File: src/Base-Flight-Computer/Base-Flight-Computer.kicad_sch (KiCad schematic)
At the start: 50 parts, among them J1 Jumper_NO, P1 1984659, P2 USB, P3 0530470610, P4 1546551-2, Q1 QS5U17TR, Q2 2N7002W-7-F, Q3 2N7002W-7-F, Q4 QS5U17TR, U1 STM32G4A1KEU6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

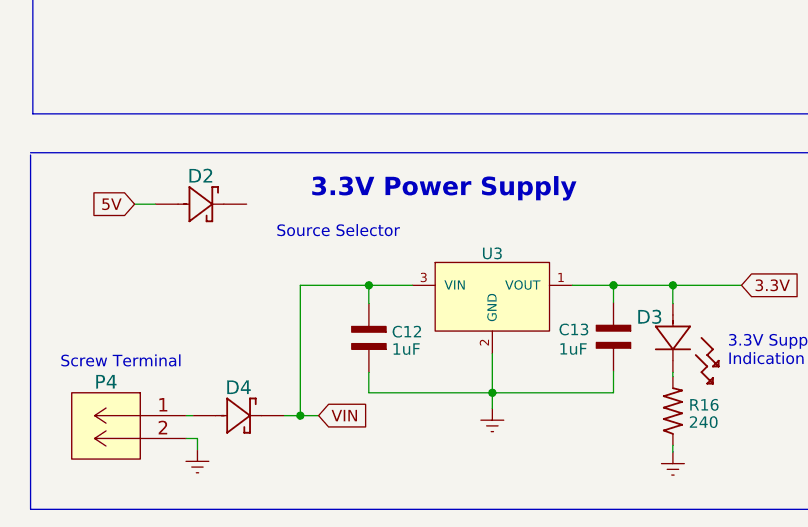
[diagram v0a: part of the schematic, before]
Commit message: added lipo batter connector to power supply circuit
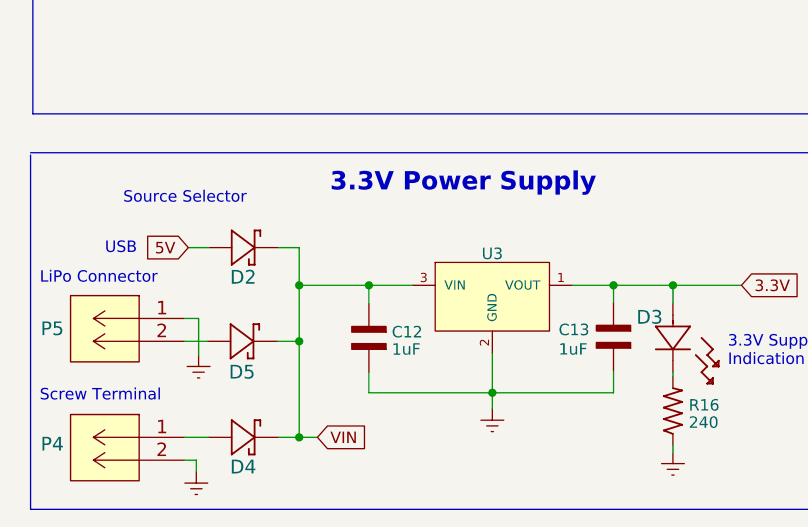
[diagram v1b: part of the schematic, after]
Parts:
- removed D2, D4: SM5819PL-TP, symbol Flight-Computer:SM5819PL-TP
- added D2, D4, D5: SM5819PL-TP, Base-Flight-Computer:SM5819PL-TP, symbol Base-Flight-Computer:SM5819PL-TP
- added P5: 1984659, Base-Flight-Computer:JST_S2B-PH-K-S(LF)(SN), symbol Base-Flight-Computer:S2B-PH-K-S__LF__SN
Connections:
- net 5V: now also D2.2
- net Earth: now also P5.1 (5)
- net VIN: now also D2.1, D4.1, D5.1
- net at P4.1 (5): now also D4.2
- new net: D5.2, P5.2 (6)
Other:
- note added: "LiPo Connector"
- moved on the sheet: P4

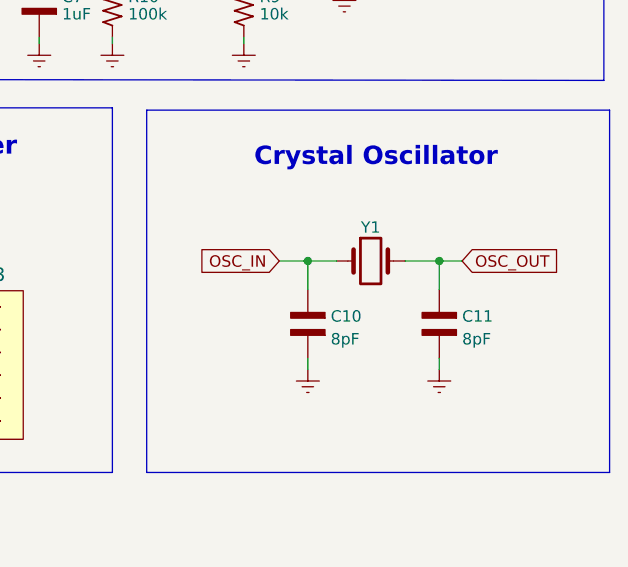
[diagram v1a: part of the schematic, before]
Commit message: reduced form factor of crystal oscillator
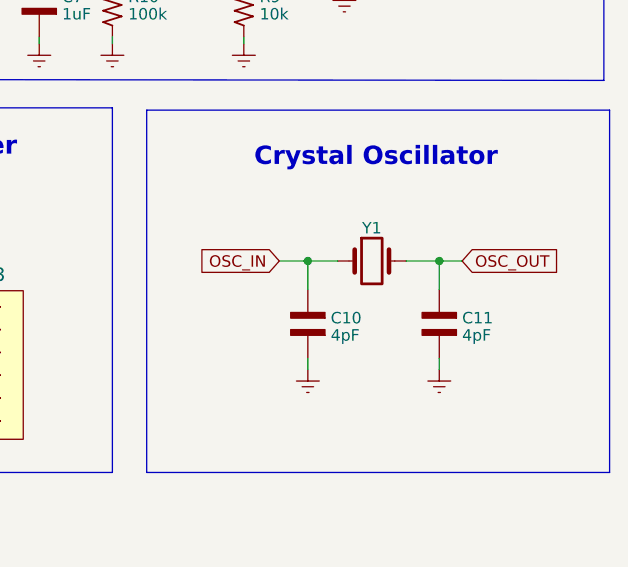
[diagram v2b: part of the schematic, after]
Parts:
- removed C10, C11: 8pF, Flight-Computer-Lite:CAP_0603, symbol Flight-Computer:CAP_0603
- removed Y1: ECS-240-18-33-JGN-TR, Flight-Computer-Lite:ECS-240-18-33-JGN-TR, symbol Flight-Computer:ECS-240-18-33-JGN-TR
- added C10, C11: 4pF, Base-Flight-Computer:CAP_0402, symbol Base-Flight-Computer:CAP_0402
- added Y1: ECS-240-18-33-JGN-TR, Base-Flight-Computer:ECS-240-12-37B-CKY-TR, symbol Base-Flight-Computer:ECS-240-12-37B-CKY-TR
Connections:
- net Earth: now also C10.2, C11.2
- net OSC_IN: now also C10.1, Y1.1
- net OSC_OUT: now also C11.1, Y1.3
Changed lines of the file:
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@@
+    (stroke (width 0) (type default))
+  )
+  (wire (pts (xy 259.969 140.97) (xy 263.652 140.97))
     (stroke (width 0) (type default))
   )
@@
     (stroke (width 0) (type default))
   )
+  (wire (pts (xy 249.047 140.97) (xy 252.349 140.97))
+    (stroke (width 0) (type default))
+  )
   (polyline (pts (xy 114.554 17.018) (xy 172.974 17.018))
     (stroke (width 0) (type default))
@@
     (stroke (width 0) (type default))
   )
-  (wire (pts (xy 259.842 140.97) (xy 263.652 140.97))
-    (stroke (width 0) (type default))
-  )
   (wire (pts (xy 199.136 148.59) (xy 204.724 148.59))
     (stroke (width 0) (type default))
@@
   )
   (wire (pts (xy 80.264 179.832) (xy 66.802 179.832))
-    (stroke (width 0) (type default))
-  )
-  (wire (pts (xy 249.047 140.97) (xy 252.222 140.97))
     (stroke (width 0) (type default))
   )
@@
     )
   )
-  (symbol (lib_id "Flight-Computer:ECS-240-18-33-JGN-TR") (at 256.032 140.97 0) (unit 1)
-    (in_bom yes) (on_board yes) (dnp no) (fields_autoplaced)
-    (property "Reference" "Y1" (at 256.032 137.2418 0)
-      (effects (font (size 1.27 1.27)))
-    )
-    (property "Value" "ECS-240-18-33-JGN-TR" (at 256.032 144.78 0)
-      (effects (font (size 1.27 1.27)) hide)
-    )
-    (property "Footprint" "Flight-Computer-Lite:ECS-240-18-33-JGN-TR" (at 256.032 140.97 0)
-      (effects (font (size 1.27 1.27)) hide)
-    )
-    (property "Datasheet" "~" (at 256.032 140.97 0)
-      (effects (font (size 1.27 1.27)) hide)
-    )
-    (pin "1")
-    (pin "2")
-    (pin "3")
-    (pin "4")
-    (instances
-      (project "Base-Flight-Computer"
-        (path "/13f33ffc-3ab1-449a-9be0-c2c7f72f3b48"
-          (reference "Y1") (unit 1)
-        )
-      )
-    )
-  )
   (symbol (lib_id "Flight-Computer:Earth") (at 227.584 73.152 0) (unit 1)
     (in_bom yes) (on_board yes) (dnp no) (fields_autoplaced)
@@
         (path "/13f33ffc-3ab1-449a-9be0-c2c7f72f3b48"
           (reference "#PWR015") (unit 1)
-        )
-      )
-    )
-  )
-  (symbol (lib_id "Flight-Computer:CAP_0603") (at 249.047 147.955 90) (unit 1)
-    (in_bom yes) (on_board yes) (dnp no) (fields_autoplaced)
-    (property "Reference" "C10" (at 251.587 147.1203 90)
-      (effects (font (size 1.27 1.27)) (justify right))
-    )
-    (property "Value" "8pF" (at 251.587 149.6572 90)
-      (effects (font (size 1.27 1.27)) (justify right))
-    )
-    (property "Footprint" "Flight-Computer-Lite:CAP_0603" (at 259.207 150.495 0)
-      (effects (font (size 1.27 1.27)) (justify left bottom) hide)
-    )
-    (property "Datasheet" "" (at 249.047 149.225 0)
-      (effects (font (size 1.27 1.27)) (justify left bottom) hide)
-    )
-    (pin "1")
-    (pin "2")
-    (instances
-      (project "Base-Flight-Computer"
-        (path "/13f33ffc-3ab1-449a-9be0-c2c7f72f3b48"
-          (reference "C10") (unit 1)
         )
       )
@@
     )
   )
-  (symbol (lib_id "Flight-Computer:CAP_0603") (at 263.652 147.955 90) (unit 1)
-    (in_bom yes) (on_board yes) (dnp no) (fields_autoplaced)
-    (property "Reference" "C11" (at 266.192 147.1203 90)
-      (effects (font (size 1.27 1.27)) (justify right))
-    )
-    (property "Value" "8pF" (at 266.192 149.6572 90)
-      (effects (font (size 1.27 1.27)) (justify right))
-    )
-    (property "Footprint" "Flight-Computer-Lite:CAP_0603" (at 273.812 150.495 0)
-      (effects (font (size 1.27 1.27)) (justify left bottom) hide)
-    )
-    (property "Datasheet" "" (at 263.652 149.225 0)
-      (effects (font (size 1.27 1.27)) (justify left bottom) hide)
-    )
-    (pin "1")
-    (pin "2")
-    (instances
-      (project "Base-Flight-Computer"
-        (path "/13f33ffc-3ab1-449a-9be0-c2c7f72f3b48"
-          (reference "C11") (unit 1)
+  (symbol (lib_id "Base-Flight-Computer:CAP_0402") (at 249.047 147.955 90) (unit 1)
+    (in_bom yes) (on_board yes) (dnp no) (fields_autoplaced)
+    (property "Reference" "C10" (at 251.587 147.3113 90)
+      (effects (font (size 1.27 1.27)) (justify right))
+    )
+    (property "Value" "4pF" (at 251.587 149.2323 90)
+      (effects (font (size 1.27 1.27)) (justify right))
+    )
+    (property "Footprint" "Base-Flight-Computer:CAP_0402" (at 259.207 150.495 0)
+      (effects (font (size 1.27 1.27)) (justify left bottom) hide)
+    )
+    (property "Datasheet" "" (at 249.047 149.225 0)
+      (effects (font (size 1.27 1.27)) (justify left bottom) hide)
+    )
+    (pin "1")
+    (pin "2")
+    (instances
+      (project "Base-Flight-Computer"
+        (path "/13f33ffc-3ab1-449a-9be0-c2c7f72f3b48"
+          (reference "C10") (unit 1)
         )
       )
@@
     )
   )
+  (symbol (lib_id "Base-Flight-Computer:CAP_0402") (at 263.652 147.955 90) (unit 1)
+    (in_bom yes) (on_board yes) (dnp no) (fields_autoplaced)
+    (property "Reference" "C11" (at 266.192 147.3113 90)
+      (effects (font (size 1.27 1.27)) (justify right))
+    )
+    (property "Value" "4pF" (at 266.192 149.2323 90)
+      (effects (font (size 1.27 1.27)) (justify right))
+    )
+    (property "Footprint" "Base-Flight-Computer:CAP_0402" (at 273.812 150.495 0)
+      (effects (font (size 1.27 1.27)) (justify left bottom) hide)
+    )
+    (property "Datasheet" "" (at 263.652 149.225 0)
+      (effects (font (size 1.27 1.27)) (justify left bottom) hide)
+    )
+    (pin "1")
+    (pin "2")
+    (instances
+      (project "Base-Flight-Computer"
+        (path "/13f33ffc-3ab1-449a-9be0-c2c7f72f3b48"
+          (reference "C11") (unit 1)
+        )
+      )
+    )
+  )
   (symbol (lib_id "Base-Flight-Computer:CAP_0402") (at 218.694 68.58 90) (unit 1)
     (in_bom yes) (on_board yes) (dnp no) (fields_autoplaced)
@@
         )
       )
+    )
+  )
+  (symbol (lib_id "Base-Flight-Computer:ECS-240-12-37B-CKY-TR") (at 256.159 140.97 0) (unit 1)
+    (in_bom yes) (on_board yes) (dnp no) (fields_autoplaced)
+    (property "Reference" "Y1" (at 256.159 137.3157 0)
+      (effects (font (size 1.27 1.27)))
+    )
+    (property "Value" "ECS-240-18-33-JGN-TR" (at 256.159 144.78 0)
+      (effects (font (size 1.27 1.27)) hide)
+    )
+    (property "Footprint" "Base-Flight-Computer:ECS-240-12-37B-CKY-TR" (at 256.159 140.97 0)
+      (effects (font (size 1.27 1.27)) hide)
+    )
+    (property "Datasheet" "~" (at 256.159 140.97 0)
+      (effects (font (size 1.27 1.27)) hide)
+    )
+    (pin "1")
+    (pin "2")
+    (pin "3")
+    (pin "4")
+    (instances
+      (project "Base-Flight-Computer"
+        (path "/13f33ffc-3ab1-449a-9be0-c2c7f72f3b48"
+          (reference "Y1") (unit 1)
+        )
+      )

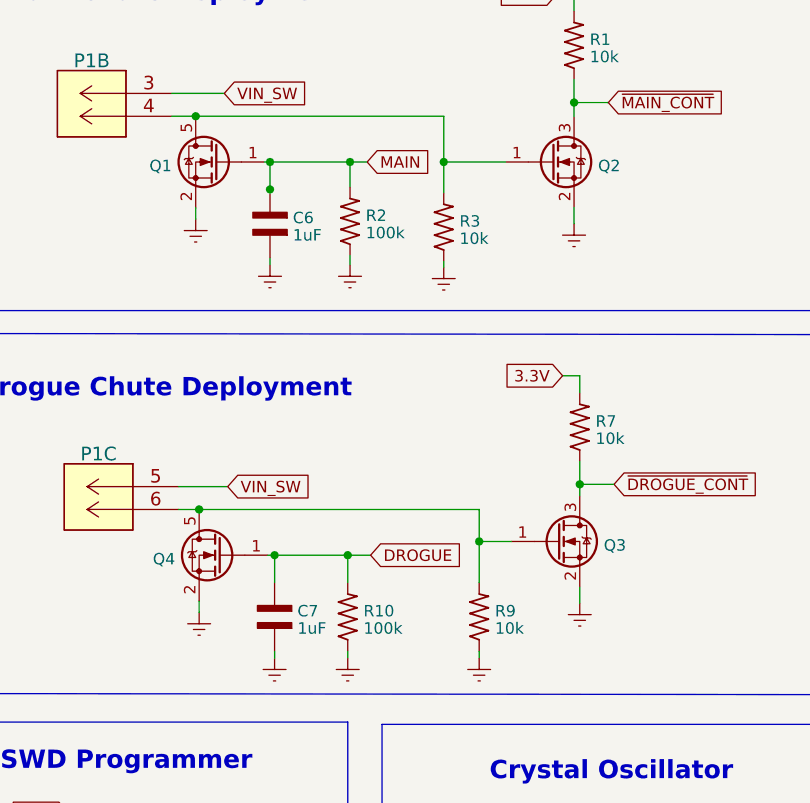
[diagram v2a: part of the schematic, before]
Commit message: changed ignition pull-down resistors to 100k to reduce parasitic ematch current
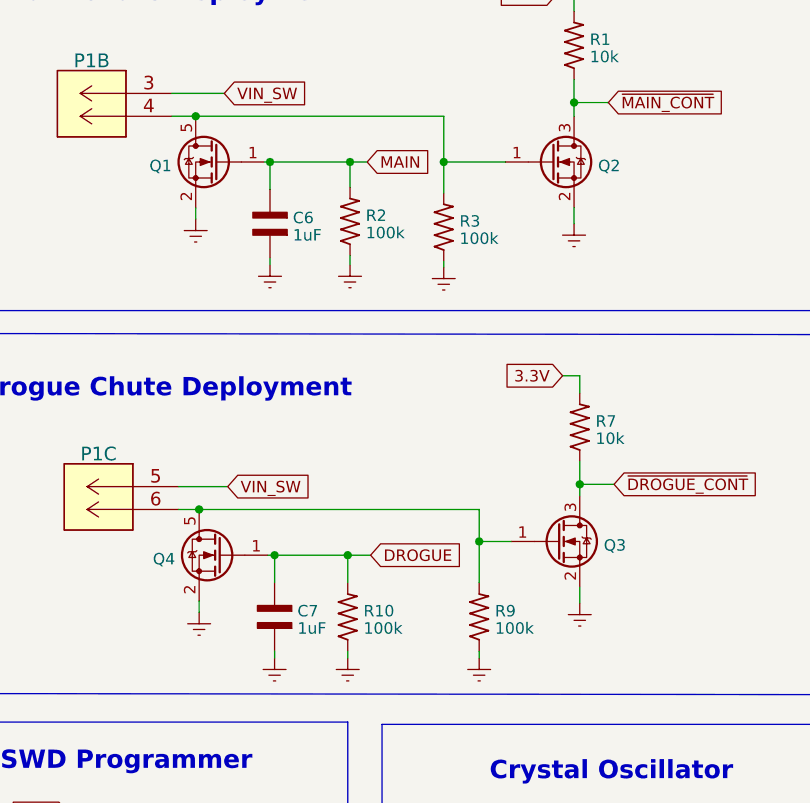
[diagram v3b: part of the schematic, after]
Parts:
- R3, R9: value 10k -> 100k

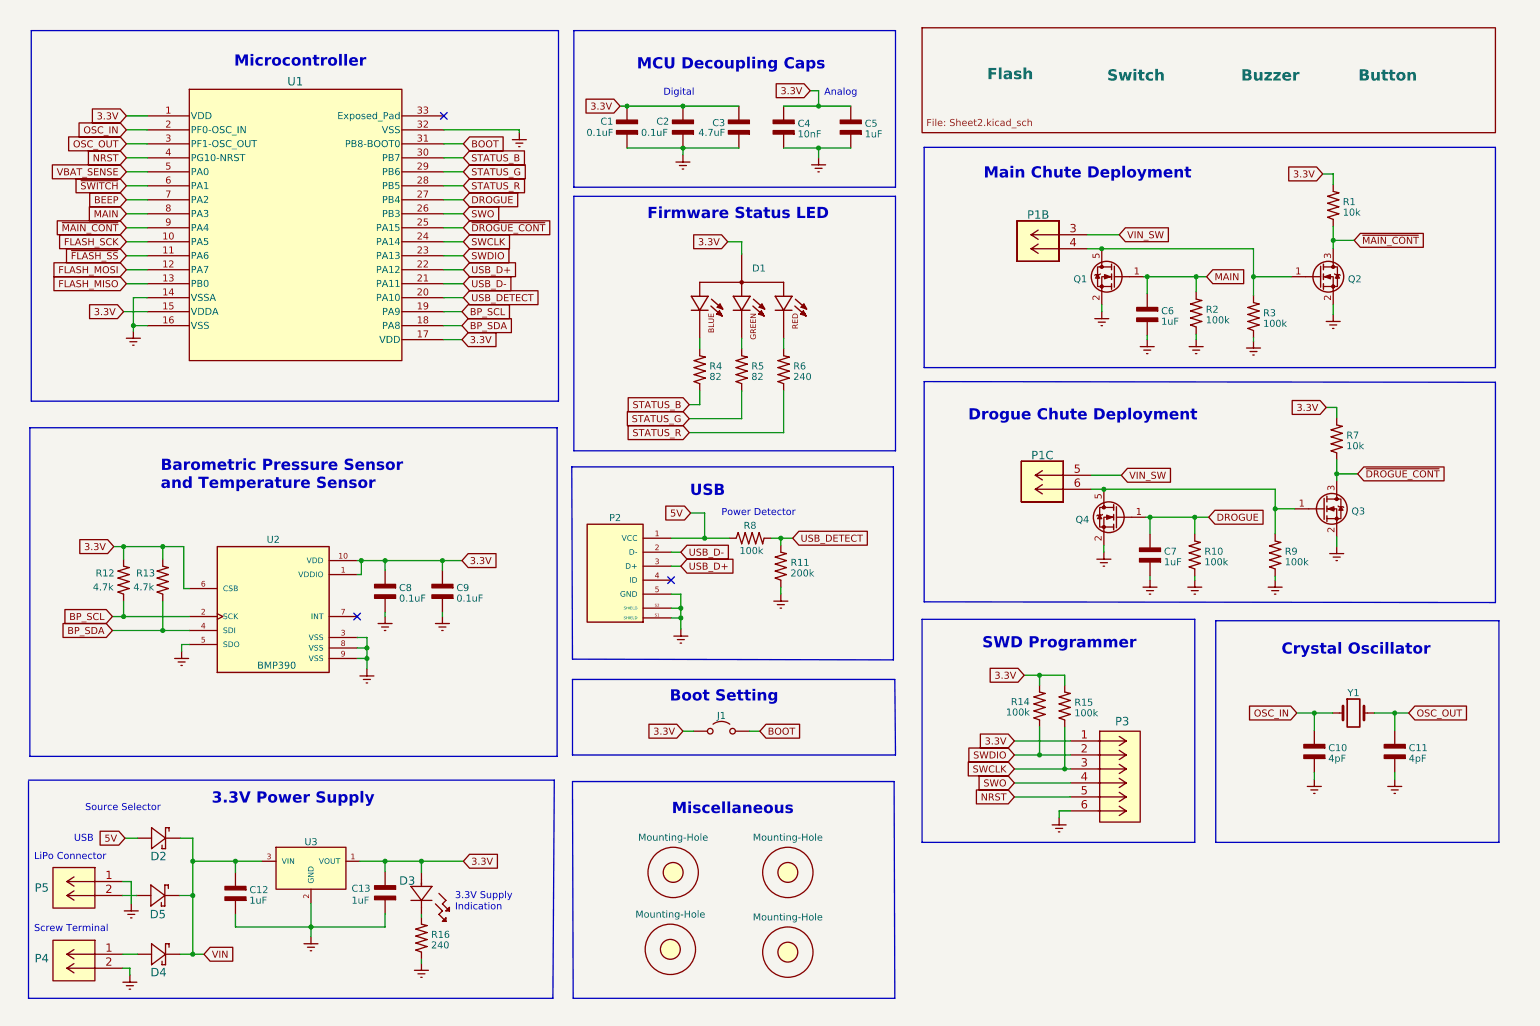
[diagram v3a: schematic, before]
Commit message: moved all components to single schematic page
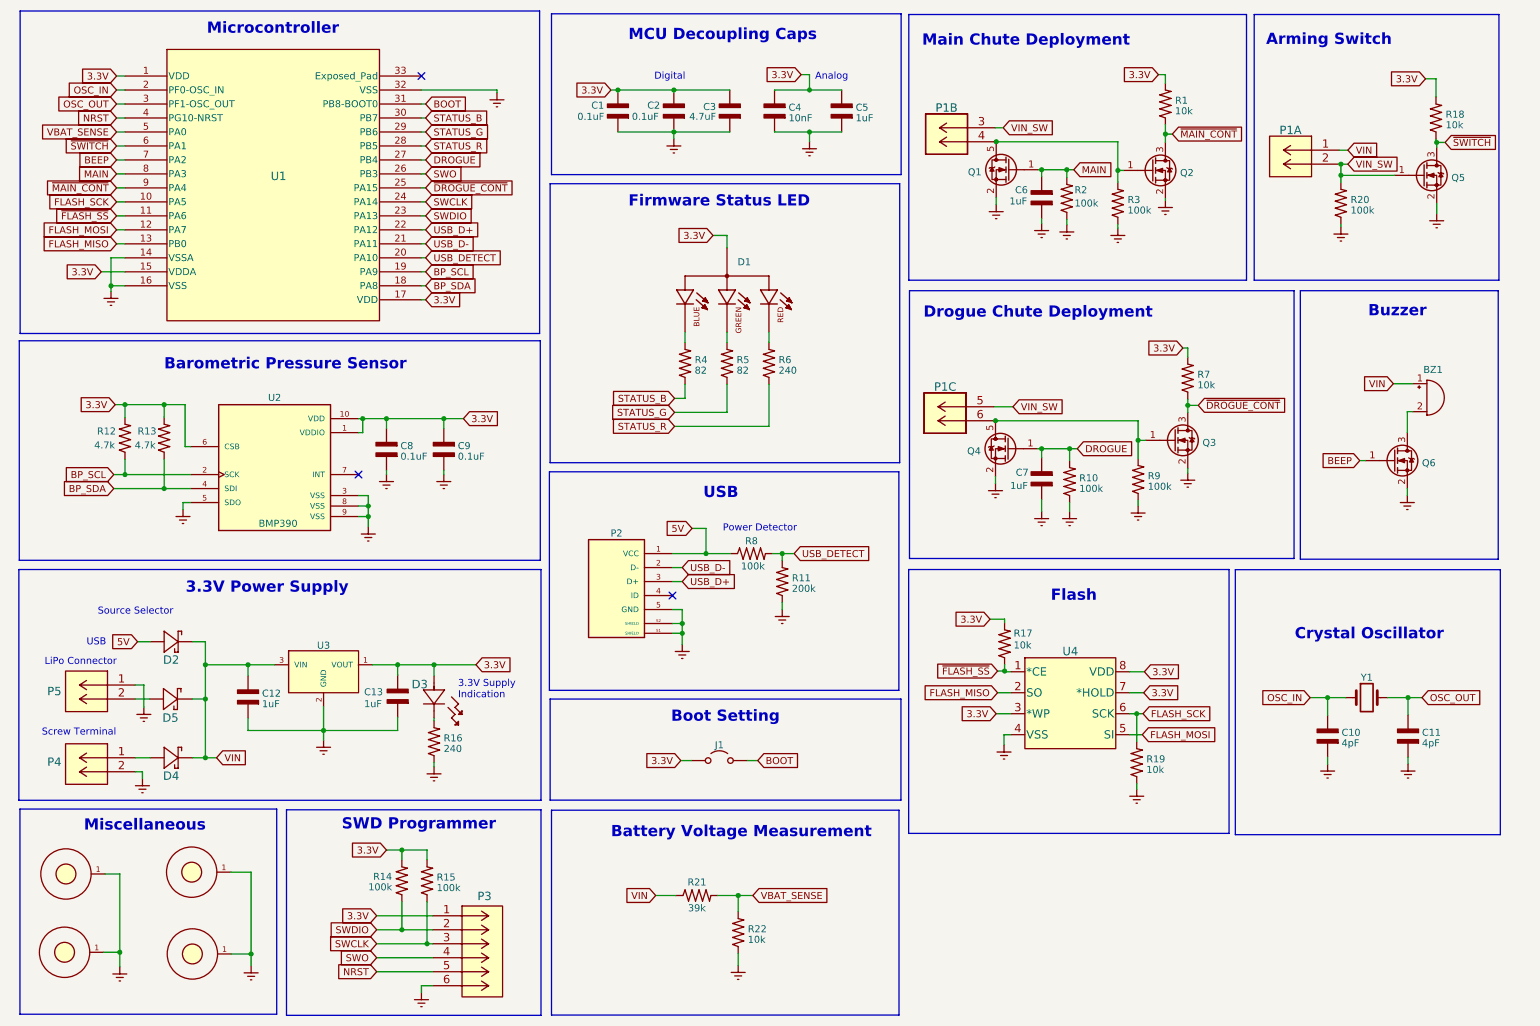
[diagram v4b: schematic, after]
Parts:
- removed H1, H2, H4: Mounting-Hole, Flight-Computer-Lite:MountingHole_3mm, symbol Flight-Computer:Mounting-Hole
- removed H3: Mounting-Hole, Flight-Computer-Lite:MountingHole_3mm, symbol Flight-Computer-Lite:Mounting-Hole
- added BZ1: AT-1438-TWT-R, Flight-Computer:AT-1438-TWT-R, symbol Flight-Computer:AT-1438-TWT-R
- added H1, H2, H3, H4: Mounting-Hole-4-40, Base-Flight-Computer:MountingHole_4-40, symbol Base-Flight-Computer:Mounting-Hole-4-40
- added unit 1 of P1
- added Q5, Q6: 2N7002W-7-F, Flight-Computer-Lite:QS5U17TR, symbol Flight-Computer-Lite:2N7002W-7-F
- added R17, R18, R19, R22: 10k, Base-Flight-Computer:RES_0402, symbol Base-Flight-Computer:RES_0402
- added R20: 100k, Base-Flight-Computer:RES_0402, symbol Base-Flight-Computer:RES_0402
- added R21: 39k, Base-Flight-Computer:RES_0402, symbol Base-Flight-Computer:RES_0402
- added U4: SST25VF040B-50-4I-S2AE-T, symbol Flight-Computer:SST25VF040B-50-4I-S2AE-T
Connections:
- net 3.3V: now also R17.2, R18.2, U4.3 (*WP), U4.7 (*HOLD), U4.8 (VDD)
- net BEEP: now also Q6.1 (G)
- net Earth: now also H1.1, H2.1, H3.1, H4.1, Q5.2 (S), Q6.2 (S), R19.1, R20.1, R22.1, U4.4 (VSS)
- net FLASH_MISO: now also U4.2 (SO)
- net FLASH_MOSI: now also U4.5 (SI)
- net FLASH_SCK: now also R19.2, U4.6 (SCK)
- net VBAT_SENSE: now also R21.2, R22.2
- net VIN: now also BZ1.1 (-), P1.1 (5), R21.1
- net VIN_SW: now also P1.2 (6), Q5.1 (G), R20.2
- net ~{FLASH_SS}: now also R17.1, U4.1 (*CE)
- net ~{SWITCH}: now also Q5.3 (D), R18.1
- new net: BZ1.2 (+), Q6.3 (D)
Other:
- removed sheet Sheet2
- note added: "Arming Switch"
- note added: "Barometric Pressure Sensor"
- note added: "Battery Voltage Measurement"
- note added: "Buzzer"
- note added: "Flash"
- note removed: "Barometric Pressure Sensor and Temperature Sensor"
- moved on the sheet: C1, C10, C11, C12, C13, C2, C3, C4, C5, C6, C7, C8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
